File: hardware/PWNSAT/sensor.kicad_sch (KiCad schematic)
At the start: 1 part, among them J3 Sensors

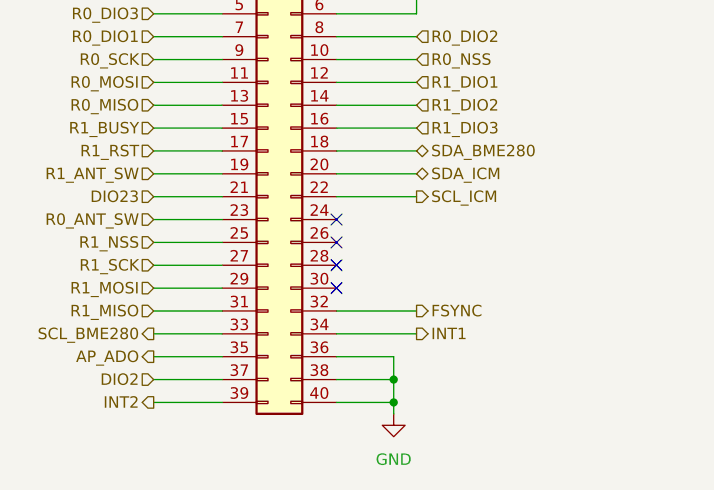
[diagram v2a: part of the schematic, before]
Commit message: feat(Hw):Route_UpdatedPWNcube_
Pending_3v3
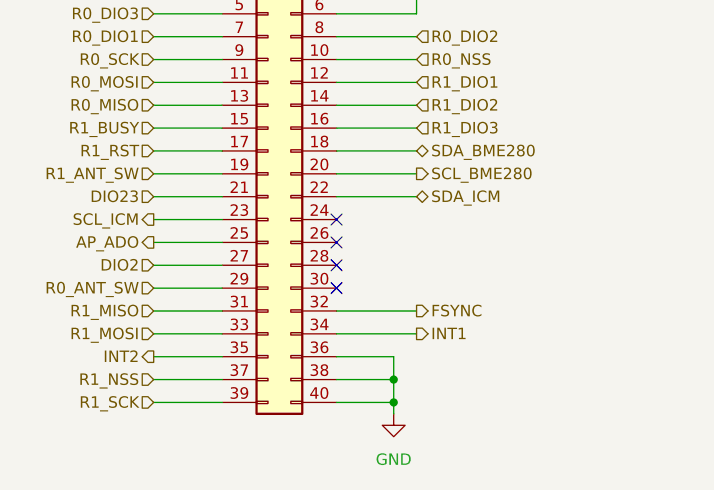
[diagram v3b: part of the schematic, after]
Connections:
- net AP_ADO: now also J3.25 (Pin_25); no longer J3.35 (Pin_35)
- net DIO2: now also J3.27 (Pin_27); no longer J3.37 (Pin_37)
- net INT2: now also J3.35 (Pin_35); no longer J3.39 (Pin_39)
- net R0_ANT_SW: now also J3.29 (Pin_29); no longer J3.23 (Pin_23)
- net R1_MOSI: now also J3.33 (Pin_33); no longer J3.29 (Pin_29)
- net R1_NSS: now also J3.37 (Pin_37); no longer J3.25 (Pin_25)
- net R1_SCK: now also J3.39 (Pin_39); no longer J3.27 (Pin_27)
- net SCL_BME280: now also J3.20 (Pin_20); no longer J3.33 (Pin_33)
- net SCL_ICM: now also J3.23 (Pin_23); no longer J3.22 (Pin_22)
- net SDA_ICM: now also J3.22 (Pin_22); no longer J3.20 (Pin_20)
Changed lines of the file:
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@@
 	(hierarchical_label "R1_SCK"
 		(shape input)
+		(at 69.85 86.36 180)
+		(effects
+			(font
+				(size 1.27 1.27)
+			)
+			(justify right)
+		)
+	)
+	(hierarchical_label "R1_MISO"
+		(shape input)
+		(at 69.85 76.2 180)
+		(effects
+			(font
+				(size 1.27 1.27)
+			)
+			(justify right)
+		)
+	)
+	(hierarchical_label "R0_NSS"
+		(shape input)
+		(at 99.06 48.26 0)
+		(effects
+			(font
+				(size 1.27 1.27)
+			)
+			(justify left)
+		)
+	)
+	(hierarchical_label "DIO2"
+		(shape input)
 		(at 69.85 71.12 180)
 		(effects
@@
 		)
 	)
-	(hierarchical_label "R1_MISO"
-		(shape input)
-		(at 69.85 76.2 180)
-		(effects
-			(font
-				(size 1.27 1.27)
-			)
-			(justify right)
-		)
-	)
-	(hierarchical_label "R0_NSS"
-		(shape input)
-		(at 99.06 48.26 0)
-		(effects
-			(font
-				(size 1.27 1.27)
-			)
-			(justify left)
-		)
-	)
-	(hierarchical_label "DIO2"
+	(hierarchical_label "INT2"
+		(shape output)
+		(at 69.85 81.28 180)
+		(effects
+			(font
+				(size 1.27 1.27)
+			)
+			(justify right)
+		)
+	)
+	(hierarchical_label "R0_MOSI"
+		(shape input)
+		(at 69.85 50.8 180)
+		(effects
+			(font
+				(size 1.27 1.27)
+			)
+			(justify right)
+		)
+	)
+	(hierarchical_label "R0_DIO3"
+		(shape input)
+		(at 69.85 43.18 180)
+		(effects
+			(font
+				(size 1.27 1.27)
+			)
+			(justify right)
+		)
+	)
+	(hierarchical_label "R0_ANT_SW"
+		(shape input)
+		(at 69.85 73.66 180)
+		(effects
+			(font
+				(size 1.27 1.27)
+			)
+			(justify right)
+		)
+	)
+	(hierarchical_label "R1_NSS"
 		(shape input)
 		(at 69.85 83.82 180)
@@
 		)
 	)
-	(hierarchical_label "INT2"
-		(shape output)
-		(at 69.85 86.36 180)
-		(effects
-			(font
-				(size 1.27 1.27)
-			)
-			(justify right)
-		)
-	)
-	(hierarchical_label "R0_MOSI"
-		(shape input)
-		(at 69.85 50.8 180)
-		(effects
-			(font
-				(size 1.27 1.27)
-			)
-			(justify right)
-		)
-	)
-	(hierarchical_label "R0_DIO3"
-		(shape input)
-		(at 69.85 43.18 180)
-		(effects
-			(font
-				(size 1.27 1.27)
-			)
-			(justify right)
-		)
-	)
-	(hierarchical_label "R0_ANT_SW"
-		(shape input)
+	(hierarchical_label "R1_MOSI"
+		(shape input)
+		(at 69.85 78.74 180)
+		(effects
+			(font
+				(size 1.27 1.27)
+			)
+			(justify right)
+		)
+	)
+	(hierarchical_label "R0_SCK"
+		(shape input)
+		(at 69.85 48.26 180)
+		(effects
+			(font
+				(size 1.27 1.27)
+			)
+			(justify right)
+		)
+	)
+	(hierarchical_label "R0_MISO"
+		(shape input)
+		(at 69.85 53.34 180)
+		(effects
+			(font
+				(size 1.27 1.27)
+			)
+			(justify right)
+		)
+	)
+	(hierarchical_label "SCL_ICM"
+		(shape output)
 		(at 69.85 66.04 180)
 		(effects
@@
 			)
 			(justify right)
-		)
-	)
-	(hierarchical_label "R1_NSS"
-		(shape input)
-		(at 69.85 68.58 180)
-		(effects
-			(font
-				(size 1.27 1.27)
-			)
-			(justify right)
-		)
-	)
-	(hierarchical_label "R1_MOSI"
-		(shape input)
-		(at 69.85 73.66 180)
-		(effects
-			(font
-				(size 1.27 1.27)
-			)
-			(justify right)
-		)
-	)
-	(hierarchical_label "R0_SCK"
-		(shape input)
-		(at 69.85 48.26 180)
-		(effects
-			(font
-				(size 1.27 1.27)
-			)
-			(justify right)
-		)
-	)
-	(hierarchical_label "R0_MISO"
-		(shape input)
-		(at 69.85 53.34 180)
-		(effects
-			(font
-				(size 1.27 1.27)
-			)
-			(justify right)
-		)
-	)
-	(hierarchical_label "SCL_ICM"
-		(shape output)
-		(at 99.06 63.5 0)
-		(effects
-			(font
-				(size 1.27 1.27)
-			)
-			(justify left)
 		)
 	)
 	(hierarchical_label "SDA_ICM"
 		(shape bidirectional)
+		(at 99.06 63.5 0)
+		(effects
+			(font
+				(size 1.27 1.27)
+			)
+			(justify left)
+		)
+	)
+	(hierarchical_label "INT1"
+		(shape output)
+		(at 99.06 78.74 0)
+		(effects
+			(font
+				(size 1.27 1.27)
+			)
+			(justify left)
+		)
+	)
+	(hierarchical_label "R1_DIO1"
+		(shape input)
+		(at 99.06 50.8 0)
+		(effects
+			(font
+				(size 1.27 1.27)
+			)
+			(justify left)
+		)
+	)
+	(hierarchical_label "DIO23"
+		(shape input)
+		(at 69.85 63.5 180)
+		(effects
+			(font
+				(size 1.27 1.27)
+			)
+			(justify right)
+		)
+	)
+	(hierarchical_label "R0_RST"
+		(shape input)
+		(at 69.85 40.64 180)
+		(effects
+			(font
+				(size 1.27 1.27)
+			)
+			(justify right)
+		)
+	)
+	(hierarchical_label "R0_DIO2"
+		(shape input)
+		(at 99.06 45.72 0)
+		(effects
+			(font
+				(size 1.27 1.27)
+			)
+			(justify left)
+		)
+	)
+	(hierarchical_label "+3.3V"
+		(shape input)
+		(at 100.33 38.1 0)
+		(effects
+			(font
+				(size 1.27 1.27)
+			)
+			(justify left)
+		)
+	)
+	(hierarchical_label "AP_ADO"
+		(shape output)
+		(at 69.85 68.58 180)
+		(effects
+			(font
+				(size 1.27 1.27)
+			)
+			(justify right)
+		)
+	)
+	(hierarchical_label "SCL_BME280"
+		(shape output)
 		(at 99.06 60.96 0)
 		(effects
@@
 		)
 	)
-	(hierarchical_label "INT1"
-		(shape output)
-		(at 99.06 78.74 0)
-		(effects
-			(font
-				(size 1.27 1.27)
-			)
-			(justify left)
-		)
-	)
-	(hierarchical_label "R1_DIO1"
-		(shape input)
-		(at 99.06 50.8 0)
-		(effects
-			(font
-				(size 1.27 1.27)
-			)
-			(justify left)
-		)
-	)
-	(hierarchical_label "DIO23"
-		(shape input)
-		(at 69.85 63.5 180)
-		(effects
-			(font
-				(size 1.27 1.27)
-			)
-			(justify right)
-		)
-	)
-	(hierarchical_label "R0_RST"
-		(shape input)
-		(at 69.85 40.64 180)
-		(effects
-			(font
-				(size 1.27 1.27)
-			)
-			(justify right)
-		)
-	)
-	(hierarchical_label "R0_DIO2"
-		(shape input)
-		(at 99.06 45.72 0)
-		(effects
-			(font
-				(size 1.27 1.27)
-			)
-			(justify left)
-		)
-	)
-	(hierarchical_label "+3.3V"
-		(shape input)
-		(at 100.33 38.1 0)
-		(effects
-			(font
-				(size 1.27 1.27)
-			)
-			(justify left)
-		)
-	)
-	(hierarchical_label "AP_ADO"
-		(shape output)
-		(at 69.85 81.28 180)
-		(effects
-			(font
-				(size 1.27 1.27)
-			)
-			(justify right)
-		)
-	)
-	(hierarchical_label "SCL_BME280"
-		(shape output)
-		(at 69.85 78.74 180)
-		(effects
-			(font
-				(size 1.27 1.27)
-			)
-			(justify right)
-		)
-	)

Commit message: feat(Hw):Boards_Updated
Pending_Sensors_Board
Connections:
- net SCL_BME280 renamed SCL_SENS
- net SCL_ICM: no longer names the net of J3.23 (Pin_23)
- net SDA_BME280 renamed SDA_SENS
- net SDA_ICM: no longer names the net of J3.22 (Pin_22)
- no-connect marks 4 -> 6
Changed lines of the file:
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@@
+	)
+	(no_connect
+		(at 77.47 66.04)
+	)
+	(no_connect
+		(at 90.17 63.5)
 	)
 	(no_connect
@@
 	(wire
 		(pts
-			(xy 99.06 63.5) (xy 90.17 63.5)
-		)
-		(stroke
-			(width 0)
-			(type default)
-		)
-	)
-	(wire
-		(pts
 			(xy 99.06 76.2) (xy 90.17 76.2)
 		)
@@
 	(wire
 		(pts
-			(xy 69.85 66.04) (xy 77.47 66.04)
-		)
-		(stroke
-			(width 0)
-			(type default)
-		)
-	)
-	(wire
-		(pts
 			(xy 90.17 38.1) (xy 99.06 38.1)
 		)
@@
 		)
 	)
+	(hierarchical_label "SCL_SENS"
+		(shape output)
+		(at 99.06 60.96 0)
+		(effects
+			(font
+				(size 1.27 1.27)
+			)
+			(justify left)
+		)
+	)
 	(hierarchical_label "R0_DIO1"
 		(shape input)
@@
 		(shape input)
 		(at 99.06 53.34 0)
-		(effects
-			(font
-				(size 1.27 1.27)
-			)
-			(justify left)
-		)
-	)
-	(hierarchical_label "SDA_BME280"
-		(shape bidirectional)
-		(at 99.06 58.42 0)
 		(effects
 			(font
@@
 		)
 	)
-	(hierarchical_label "SCL_ICM"
-		(shape output)
-		(at 69.85 66.04 180)
-		(effects
-			(font
-				(size 1.27 1.27)
-			)
-			(justify right)
-		)
-	)
-	(hierarchical_label "SDA_ICM"
+	(hierarchical_label "SDA_SENS"
 		(shape bidirectional)
-		(at 99.06 63.5 0)
+		(at 99.06 58.42 0)
 		(effects
 			(font
@@
 		)
 	)
-	(hierarchical_label "SCL_BME280"
-		(shape output)
-		(at 99.06 60.96 0)
-		(effects
-			(font
-				(size 1.27 1.27)
-			)
-			(justify left)
-		)
-	)

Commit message: feat(Hw):BoM´s_Updated
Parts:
- J3: LCSC# (none) -> C7501249
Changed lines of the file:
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@@
+			)
+		)
+		(property "Proveedor" ""
+			(at 82.55 60.96 0)
+			(effects
+				(font
+					(size 1.27 1.27)
+				)
+				(hide yes)
+			)
+		)
+		(property "LCSC#" "C7501249"
+			(at 82.55 60.96 0)
+			(effects
+				(font
+					(size 1.27 1.27)
+				)
+				(hide yes)
 			)
 		)
